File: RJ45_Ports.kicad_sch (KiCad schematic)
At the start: 17 parts, among them J2 R-RJ45R10P-B000, J3 R-RJ45R10P-B000

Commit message: 1
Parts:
- renumbered C6 to C38, C7 to C39, C8 to C41, C9 to C43, C12 to C46, C11 to C47, J2 to J1, J3 to J2, R5 to R21, R12 to R22, R6 to R23, R11 to R24, R7 to R25, R10 to R26, R8 to R27, R9 to R29
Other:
- moved on the sheet: C38, C39, C41, C43, C46, C47, J1, J2, R21, R22, R23, R24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

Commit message: add ci
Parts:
- TR1: symbol Transformer:PT61020EL -> PoE_Splitter:TG2498S
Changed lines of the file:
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@@
 	)
 	(symbol
-		(lib_id "Transformer:PT61020EL")
+		(lib_id "PoE_Splitter:TG2498S")
 		(at 146.05 76.2 0)
 		(unit 1)
@@
 			(effects
 				(font
-					(size 1.016 1.016)
+					(size 1.27 1.27)
 				)
 			)
 		)
-		(property "Datasheet" "https://www.bourns.com/pdfs/PT61020.pdf"
+		(property "Datasheet" "https://www.lcsc.com/datasheet/C37328808.pdf"
 			(at 146.05 76.2 0)
 			(hide yes)
@@
 			(effects
 				(font
-					(size 1.016 1.016)
+					(size 1.27 1.27)
 				)
 			)
 		)
-		(property "Description" "10/100/1000 Base-T Ethernet Transformer, SMD-24"
+		(property "Description" "10GBASE-T POE+ Transformer Module, TG2498S"
 			(at 146.05 76.2 0)
 			(hide yes)
@@
 			(effects
 				(font
-					(size 1.016 1.016)
+					(size 1.27 1.27)
 				)
 			)

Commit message: add sheet titles
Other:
- company: (none) -> Acha
- title: (none) -> PoE_Splitter
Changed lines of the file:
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@@
 	(generator_version "10.0")
 	(paper "A4")
+	(title_block
+		(title "PoE_Splitter")
+		(date "${CURRENT_DATE}")
+		(rev "${SHORT_SHA}")
+		(company "Acha")
+		(comment 1 "https://github.com/acha666/PoE_Splitter@${BRANCH}")
+		(comment 2 "GPL-3.0 Licensed")
+	)
 	(junction
 		(at 168.91 110.49)

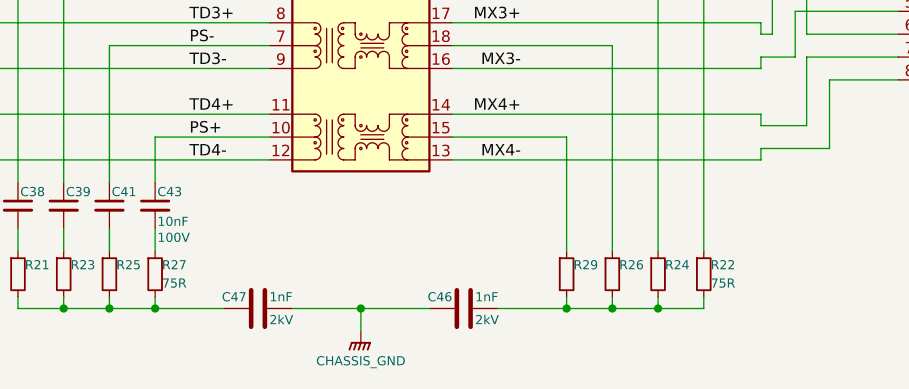
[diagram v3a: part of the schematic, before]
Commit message: MPQ boost cap value MPQ PG pull-up res all res value unit naming
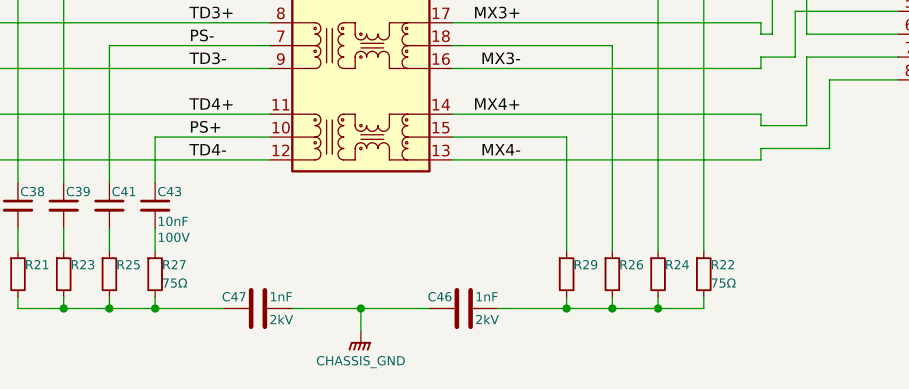
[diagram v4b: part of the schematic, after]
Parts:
- R21, R22, R23, R24, R25, R26, R27, R29: value 75R -> 75Ω
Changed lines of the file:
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@@
 			)
 		)
-		(property "Value" "75R"
+		(property "Value" "75Ω"
 			(at 179.832 107.696 0)
 			(hide yes)
@@
 			)
 		)
-		(property "Value" "75R"
+		(property "Value" "75Ω"
 			(at 169.672 107.696 0)
 			(hide yes)
@@
 			)
 		)
-		(property "Value" "75R"
+		(property "Value" "75Ω"
 			(at 113.792 107.696 0)
 			(hide yes)
@@
 			)
 		)
-		(property "Value" "75R"
+		(property "Value" "75Ω"
 			(at 184.912 107.696 0)
 			(show_name no)
@@
 			)
 		)
-		(property "Value" "75R"
+		(property "Value" "75Ω"
 			(at 118.872 107.696 0)
 			(hide yes)
@@
 			)
 		)
-		(property "Value" "75R"
+		(property "Value" "75Ω"
 			(at 123.952 107.696 0)
 			(show_name no)
@@
 			)
 		)
-		(property "Value" "75R"
+		(property "Value" "75Ω"
 			(at 174.752 107.696 0)
 			(hide yes)
@@
 			)
 		)
-		(property "Value" "75R"
+		(property "Value" "75Ω"
 			(at 108.712 107.696 0)
 			(hide yes)
